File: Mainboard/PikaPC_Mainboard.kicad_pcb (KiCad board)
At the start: 2 copper layers, 190.5 x 147.3 mm, 88 parts, among them J1 Conn_02x05_Odd_Even, J10 Conn_01x08, J11 Conn_01x08, J12 Conn_01x08, J13 Conn_01x08, J14 Conn_01x08, J15 Conn_01x08, J16 Conn_01x08, J17 Conn_01x08, J18 Conn_01x10, J19 Conn_02x05_Odd_Even, J5 DIN41612_03x32_C_Split, J6 Mini-DIN-6, J7 Mini-DIN-6, J8 Conn_01x06, J9 Conn_01x08, SW1 SW_Push_DPDT, SW2 SW_Push, U1 PPC403GA, U10 74LS07, U11 86C325, U12 GD75232N, U13 74LVC125, U14 MCP120-315GI/TO, U15 AS6C4008-55PCN, U16 AS6C4008-55PCN, U17 ATF1504, U18 T224162B, U19 T224162B, U2 SN74LVC245A, U20 T224162B, U21 T224162B, U3 SST39VF010, U4 SN74LVC245A, U5 SN74LVC245A, U6 SN74LVC245A, U7 8042 PS/2, U8 ATF22V10C, U9 74LS04, Y1 25M, Y2 7M3728, Y3 14M31818

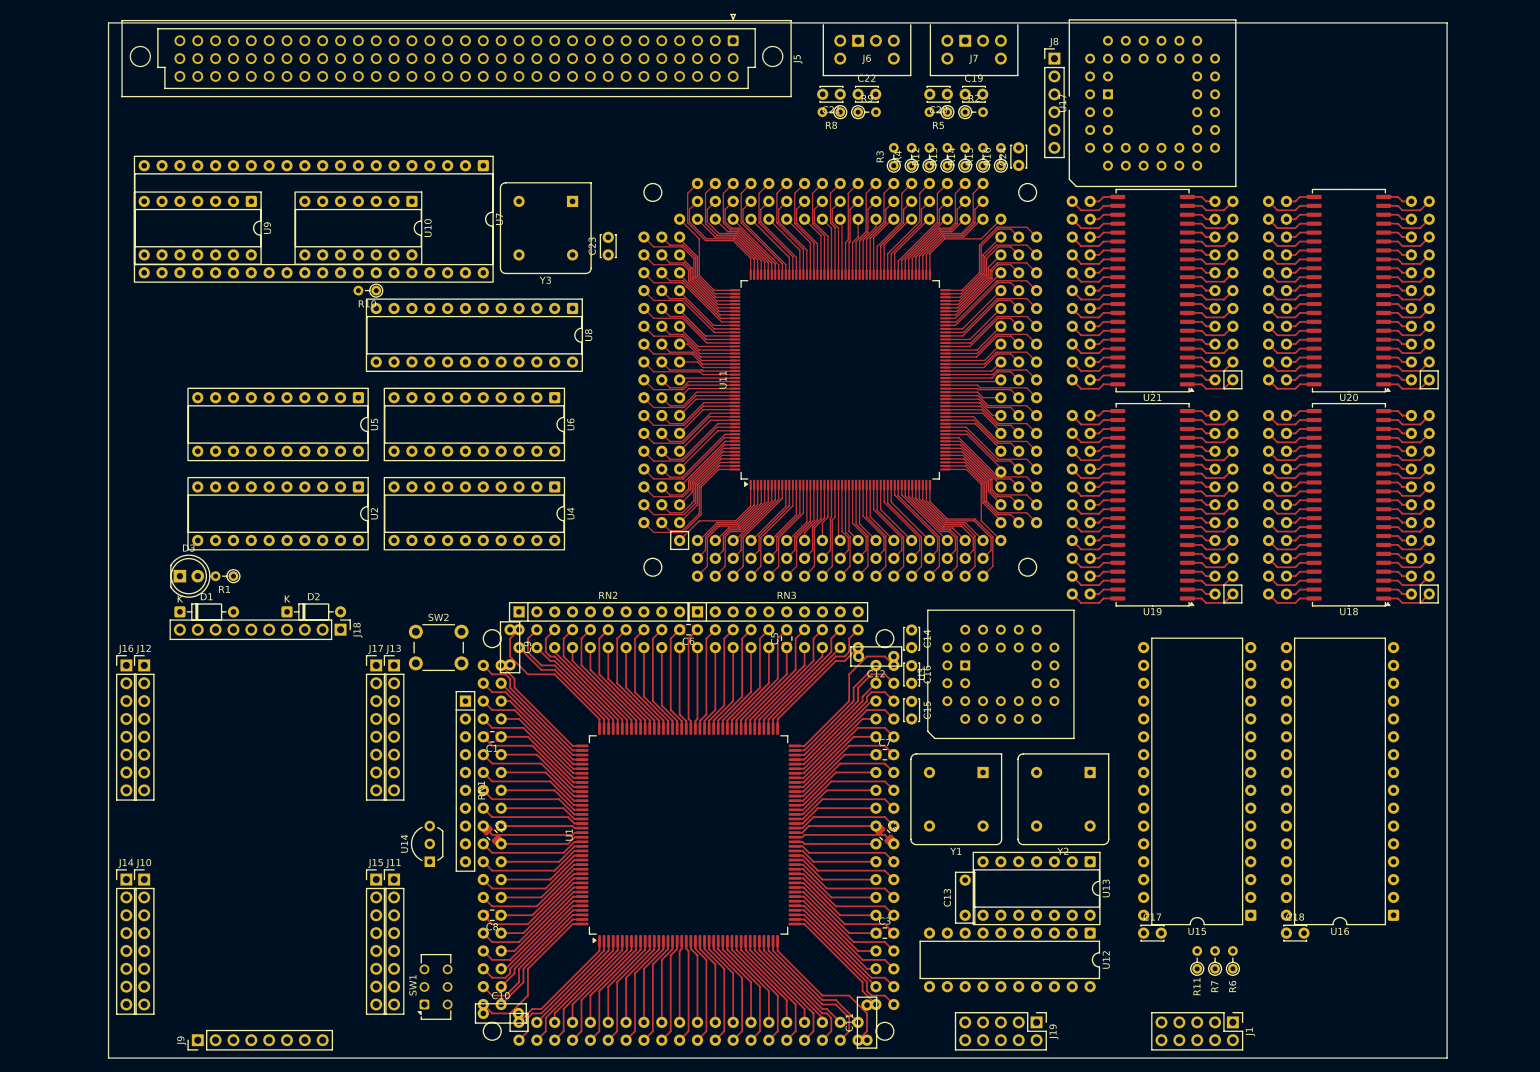
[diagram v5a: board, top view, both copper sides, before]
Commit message: cleanup keyboard logic
- odds & ends found while wiring
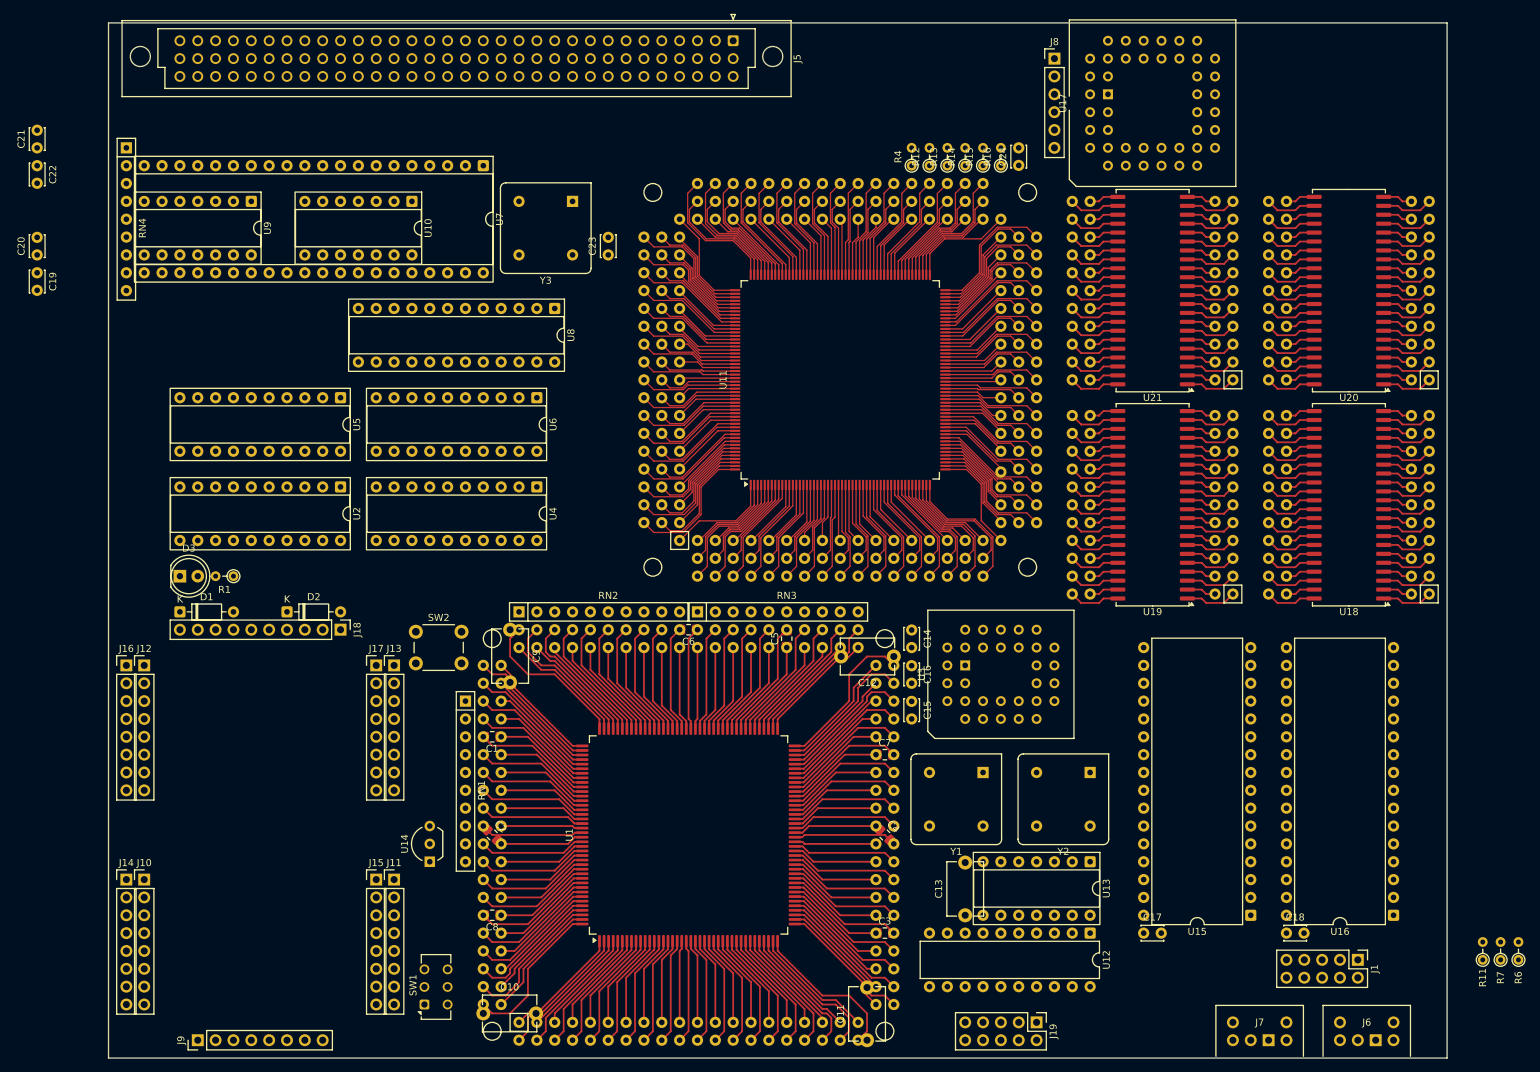
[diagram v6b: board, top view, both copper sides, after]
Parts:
- removed R10, R3: 4k7, Resistor_THT:R_Axial_DIN0204_L3.6mm_D1.6mm_P2.54mm_Vertical
- removed R2, R5, R8, R9: 10k, Resistor_THT:R_Axial_DIN0204_L3.6mm_D1.6mm_P2.54mm_Vertical
- added RN4: 9A103J, Resistor_THT:R_Array_SIP9, F.Cu at (73.7, 30.5)
- C10, C11, C12, C13, C9: footprint Capacitor_THT:C_Disc_D7.0mm_W2.5mm_P5.00mm -> Capacitor_THT:C_Disc_D7.5mm_W5.0mm_P7.50mm
- moved J6 163.6 mm to (250.2, 160.0), turned to 180 degrees
- moved J7 152.8 mm to (234.9, 160.0), turned to 180 degrees
- moved C19 134.5 mm to (61.0, 48.3), turned to -90 degrees
- moved C20 131.5 mm to (61.0, 45.7), turned to 90 degrees
- moved C22 117.3 mm to (61.0, 33.0), turned to -90 degrees
- moved C21 114.6 mm to (61.0, 30.5), turned to 90 degrees
- moved R7 40.7 mm to (269.2, 146.0)
- moved R11 40.7 mm to (266.7, 146.0)
- moved R6 40.7 mm to (271.8, 146.0)
- moved J1 19.9 mm to (248.9, 146.0)
- moved U5 2.54 mm to (104.1, 66.0)
- moved U2 2.54 mm to (104.1, 78.7)
- moved U4 2.54 mm to (132.1, 78.7)
- moved U6 2.54 mm to (132.1, 66.0)
- moved U8 2.54 mm to (134.6, 53.3)
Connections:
- net /SDReady renamed /~{SDReady}
- U10 pad 10: /~{Reset-5v} -> unconnected-(U10-Pad10)
- U10 pad 11: /~{Reset} -> unconnected-(U10-Pad11)
- U11 pad 193: /~{Reset-5v} -> /~{Reset}
- U13 pad 1: /PDReady -> /~{VID-SRDYn}
- U8 pad 15: /~{VID-ADS} -> unconnected-(U8-IO15-Pad15)
- U8 pad 16: unconnected-(U8-IO16-Pad16) -> /~{VID-ADS}
- U8 pad 17: /~{VID-SBE3} -> /~{VID-SBE0}
- U8 pad 18: /~{VID-SBE2} -> /~{VID-SBE1}
- U8 pad 19: /~{VID-SBE1} -> /~{VID-SBE2}
- U8 pad 20: /~{VID-SBE0} -> /~{VID-SBE3}
- U8 pad 22: /Ready-5v -> /PDReady
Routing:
- net /~{Reset}: track 13.7 -> 28.8 mm
- net /~{Reset-5v}: track 15.1 -> 0.00 mm

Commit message: Invert system clock to ViRGE
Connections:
- U11 pad 194: /SysClk-5v -> /~{SysClk-5v}
- U9 pad 12: unconnected-(U9-Pad12) -> /~{SysClk-5v}
- U9 pad 13: unconnected-(U9-Pad13) -> /SysClk-5v
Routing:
- net /~{SysClk-5v}: track 0.00 -> 9.72 mm
- net /SysClk-5v: track 9.72 -> 0.00 mm

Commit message: ViRGE schematic/layout cleanup
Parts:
- removed R12, R13, R14, R15, R16: 10k, Resistor_THT:R_Axial_DIN0204_L3.6mm_D1.6mm_P2.54mm_Vertical
- removed R4: 147R, Resistor_THT:R_Axial_DIN0204_L3.6mm_D1.6mm_P2.54mm_Vertical
- added R2: 220R, Resistor_THT:R_Axial_DIN0204_L3.6mm_D1.6mm_P2.54mm_Vertical, F.Cu at (142.2, 53.3)
- added R3: 470R, Resistor_THT:R_Axial_DIN0204_L3.6mm_D1.6mm_P2.54mm_Vertical, F.Cu at (142.2, 58.4)
- added RN5: 9A103J, Resistor_THT:R_Array_SIP9, F.Cu at (142.2, 61.0)
- moved U20 41.3 mm to (219.7, 81.3)
- moved J8 41.0 mm to (210.8, -22.9)
- moved U17 41.0 mm to (218.4, -17.8)
- moved U19 35.6 mm to (219.7, 45.7)
- moved U21 28.4 mm to (247.7, 45.7)
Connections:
- RN3 pad 3: /INT0 -> unconnected-(RN3-R2-Pad3)
- RN3 pad 4: /INT1 -> unconnected-(RN3-R3-Pad4)
- RN3 pad 5: /INT2 -> unconnected-(RN3-R4-Pad5)
- U7 pad 35: unconnected-(U7-KB-OBFO-Pad35) -> /INT1
- U7 pad 36: unconnected-(U7-MS-OBFO-Pad36) -> /INT2
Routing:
- net /PD23: track 31.7 -> 15.9 mm
- net +5V: track 302.5 -> 318.4 mm
- net /PD22: track 20.0 -> 10.0 mm
- net /VMD19: track 4.20 -> 14.2 mm
